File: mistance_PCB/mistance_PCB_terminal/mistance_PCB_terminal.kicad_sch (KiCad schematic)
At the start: 51 parts, among them J1 SMA-J-P-X-ST-TH1, Q1 Q_PMOS_DSG, U1 AMS1117-3.3, U2 STM32F103C8T6, U3 MCP73831-2-OT, U4 CP2104, U5 TPS61200DRC, U6 USBLC6-2P6, U7 SX1278, Y1 Crystal

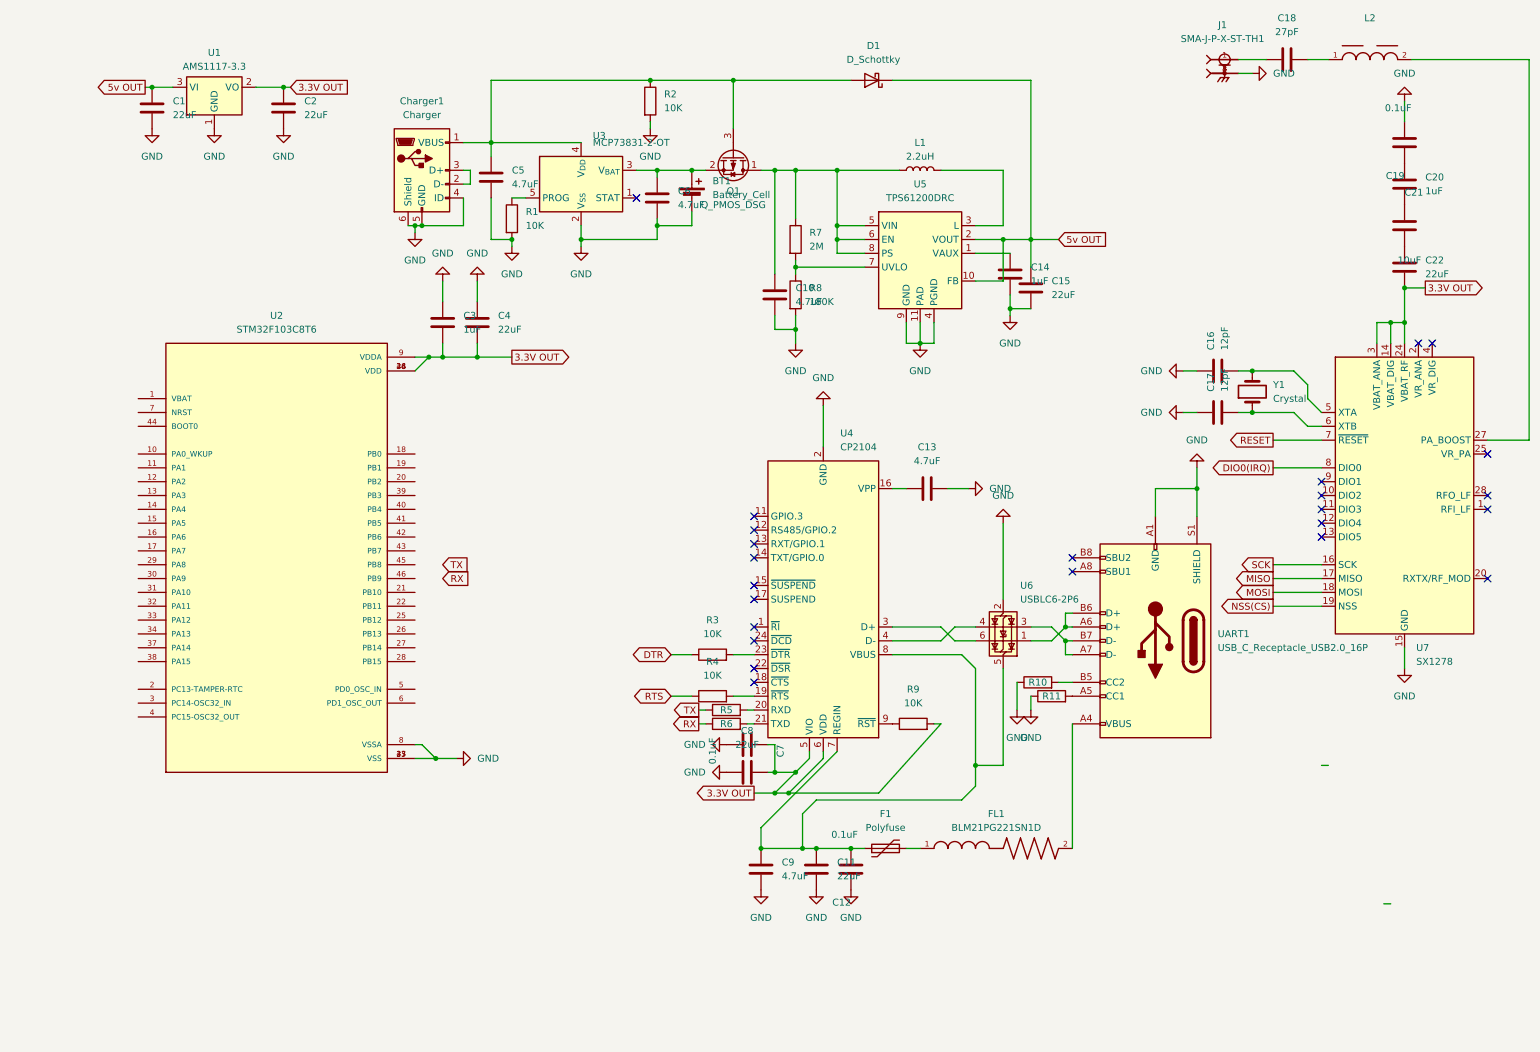
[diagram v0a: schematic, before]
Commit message: modify terminal SCH
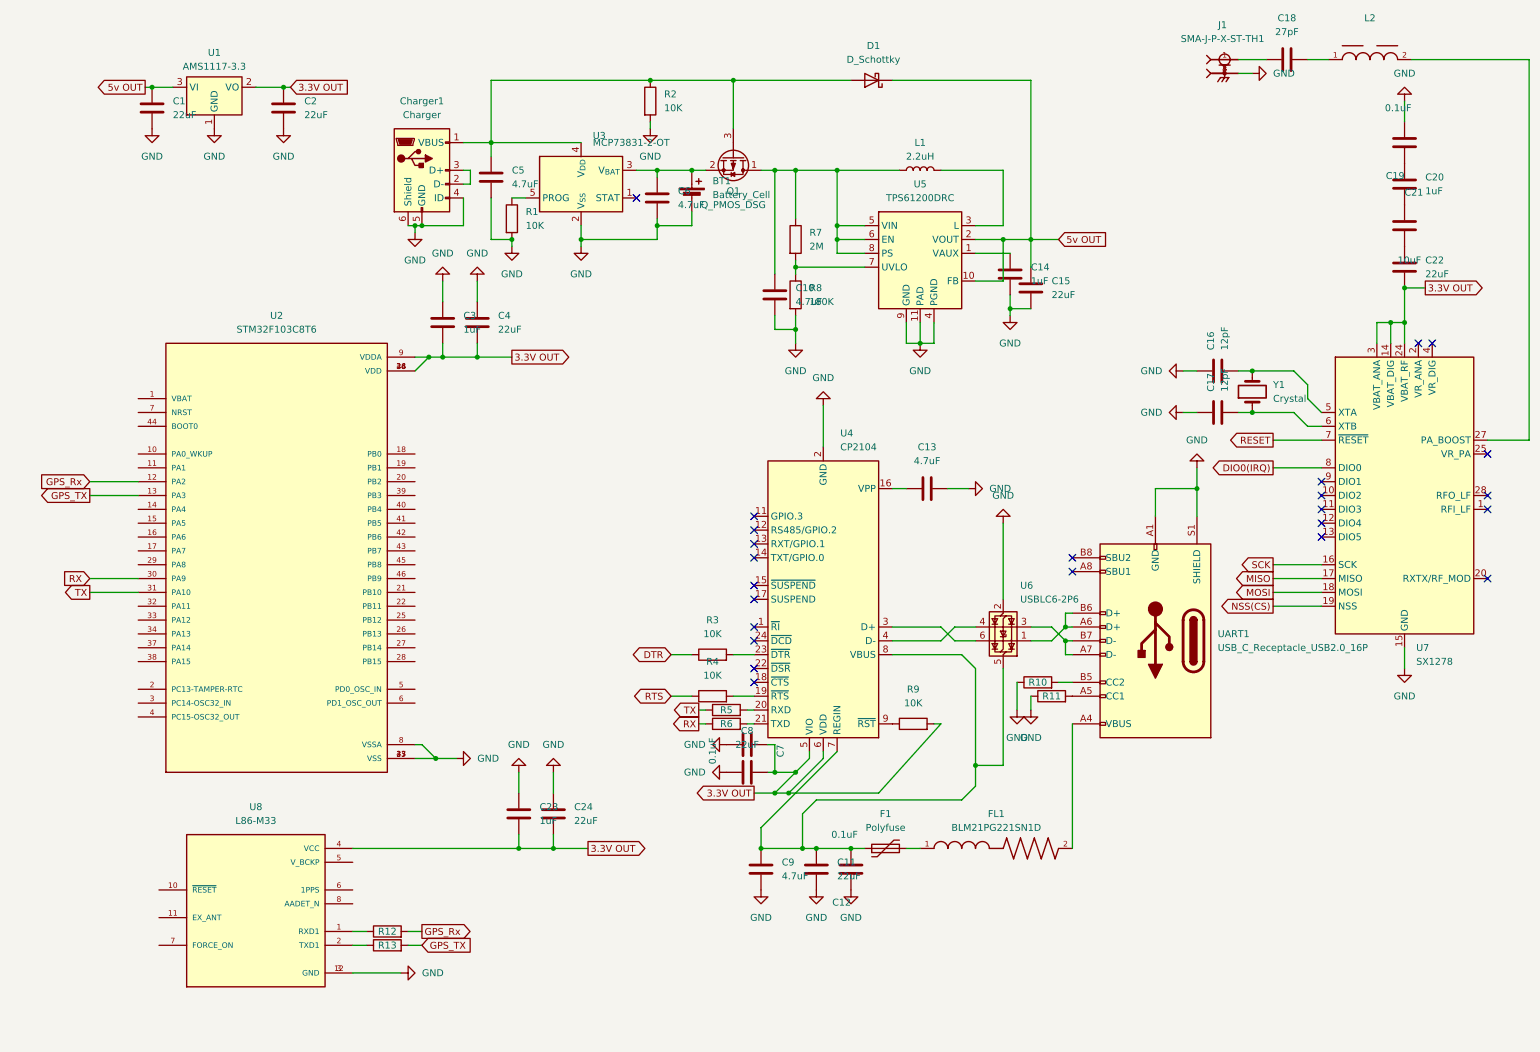
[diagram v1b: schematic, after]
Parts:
- added C23: 1uF, Capacitor_SMD:C_0603_1608Metric, symbol Device:C
- added C24: 22uF, Capacitor_SMD:C_0805_2012Metric, symbol Device:C
- added R12, R13: 22R, Resistor_SMD:R_0402_1005Metric, symbol Device:R
- added U8: L86-M33, L86-M33:XCVR_L86-M33, symbol L86-M33:L86-M33
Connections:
- net 3.3V OUT: now also C23.2, C24.2, U8.4 (VCC)
- net GND: now also C23.1, C24.1, U8.12 (GND), U8.3 (GND)
- net RX: now also U2.30 (PA9)
- net TX: now also U2.31 (PA10)
- net GPS_Rx: now reaches U2.12 (PA2)
- net GPS_Rx: now also R12.2
- net GPS_TX: now reaches U2.13 (PA3)
- net GPS_TX: now also R13.2
- new net: R12.1, U8.1 (RXD1)
- new net: R13.1, U8.2 (TXD1)

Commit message: modify terminal SCH
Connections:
- net 3.3V OUT: now also U8.5 (V_BCKP)
- net GPS_Reset: now reaches U2.11 (PA1)
- net GPS_Reset: now also U8.10 (~{RESET})
- no-connect marks 24 -> 28
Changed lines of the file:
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@@
+	)
+	(junction
+		(at 68.58 161.29)
+		(diameter 0)
+		(color 0 0 0 0)
 	)
 	(junction
@@
 	)
 	(no_connect
+		(at 66.04 168.91)
+	)
+	(no_connect
 		(at 274.32 111.76)
 	)
@@
 	)
 	(no_connect
+		(at 66.04 171.45)
+	)
+	(no_connect
 		(at 274.32 96.52)
 	)
@@
 	)
 	(no_connect
+		(at 30.48 173.99)
+	)
+	(no_connect
 		(at 139.7 123.19)
 	)
 	(no_connect
+		(at 30.48 179.07)
+	)
+	(no_connect
 		(at 243.84 93.98)
 	)
@@
 	(wire
 		(pts
-			(xy 66.04 161.29) (xy 96.52 161.29)
+			(xy 66.04 161.29) (xy 68.58 161.29)
 		)
 		(stroke
@@
 	(wire
 		(pts
+			(xy 68.58 161.29) (xy 96.52 161.29)
+		)
+		(stroke
+			(width 0)
+			(type default)
+		)
+	)
+	(wire
+		(pts
 			(xy 152.4 80.01) (xy 152.4 87.63)
 		)
@@
 	(wire
 		(pts
+			(xy 68.58 161.29) (xy 66.04 163.83)
+		)
+		(stroke
+			(width 0)
+			(type default)
+		)
+	)
+	(wire
+		(pts
 			(xy 95.25 41.91) (xy 97.79 41.91)
 		)
@@
 	(wire
 		(pts
+			(xy 25.4 168.91) (xy 30.48 168.91)
+		)
+		(stroke
+			(width 0)
+			(type default)
+		)
+	)
+	(wire
+		(pts
 			(xy 81.28 144.78) (xy 85.09 144.78)
 		)
@@
 		(pts
 			(xy 180.34 52.07) (xy 186.69 52.07)
+		)
+		(stroke
+			(width 0)
+			(type default)
+		)
+	)
+	(wire
+		(pts
+			(xy 17.78 91.44) (xy 26.67 91.44)
 		)
 		(stroke
@@
 	)
 	(global_label "TX"
-		(shape output)
+		(shape input)
 		(at 17.78 114.3 180)
 		(fields_autoplaced yes)
@@
 	)
 	(global_label "RX"
-		(shape input)
+		(shape output)
 		(at 17.78 111.76 180)
 		(fields_autoplaced yes)
@@
 		)
 	)
+	(global_label "GPS_Reset"
+		(shape input)
+		(at 17.78 91.44 180)
+		(fields_autoplaced yes)
+		(effects
+			(font
+				(size 1.27 1.27)
+			)
+			(justify right)
+		)
+		(property "Intersheetrefs" "${INTERSHEET_REFS}"
+			(at 4.8767 91.44 0)
+			(effects
+				(font
+					(size 1.27 1.27)
+				)
+				(justify right)
+				(hide yes)
+			)
+		)
+	)
 	(global_label "MISO"
 		(shape output)
@@
 		)
 	)
+	(global_label "GPS_Reset"
+		(shape output)
+		(at 25.4 168.91 180)
+		(fields_autoplaced yes)
+		(effects
+			(font
+				(size 1.27 1.27)
+			)
+			(justify right)
+		)
+		(property "Intersheetrefs" "${INTERSHEET_REFS}"
+			(at 12.4967 168.91 0)
+			(effects
+				(font
+					(size 1.27 1.27)
+				)
+				(justify right)
+				(hide yes)
+			)
+		)
+	)
 	(global_label "RTS"
 		(shape bidirectional)
@@
 	)
 	(global_label "RX"
-		(shape output)
+		(shape input)
 		(at 129.54 138.43 180)
 		(fields_autoplaced yes)

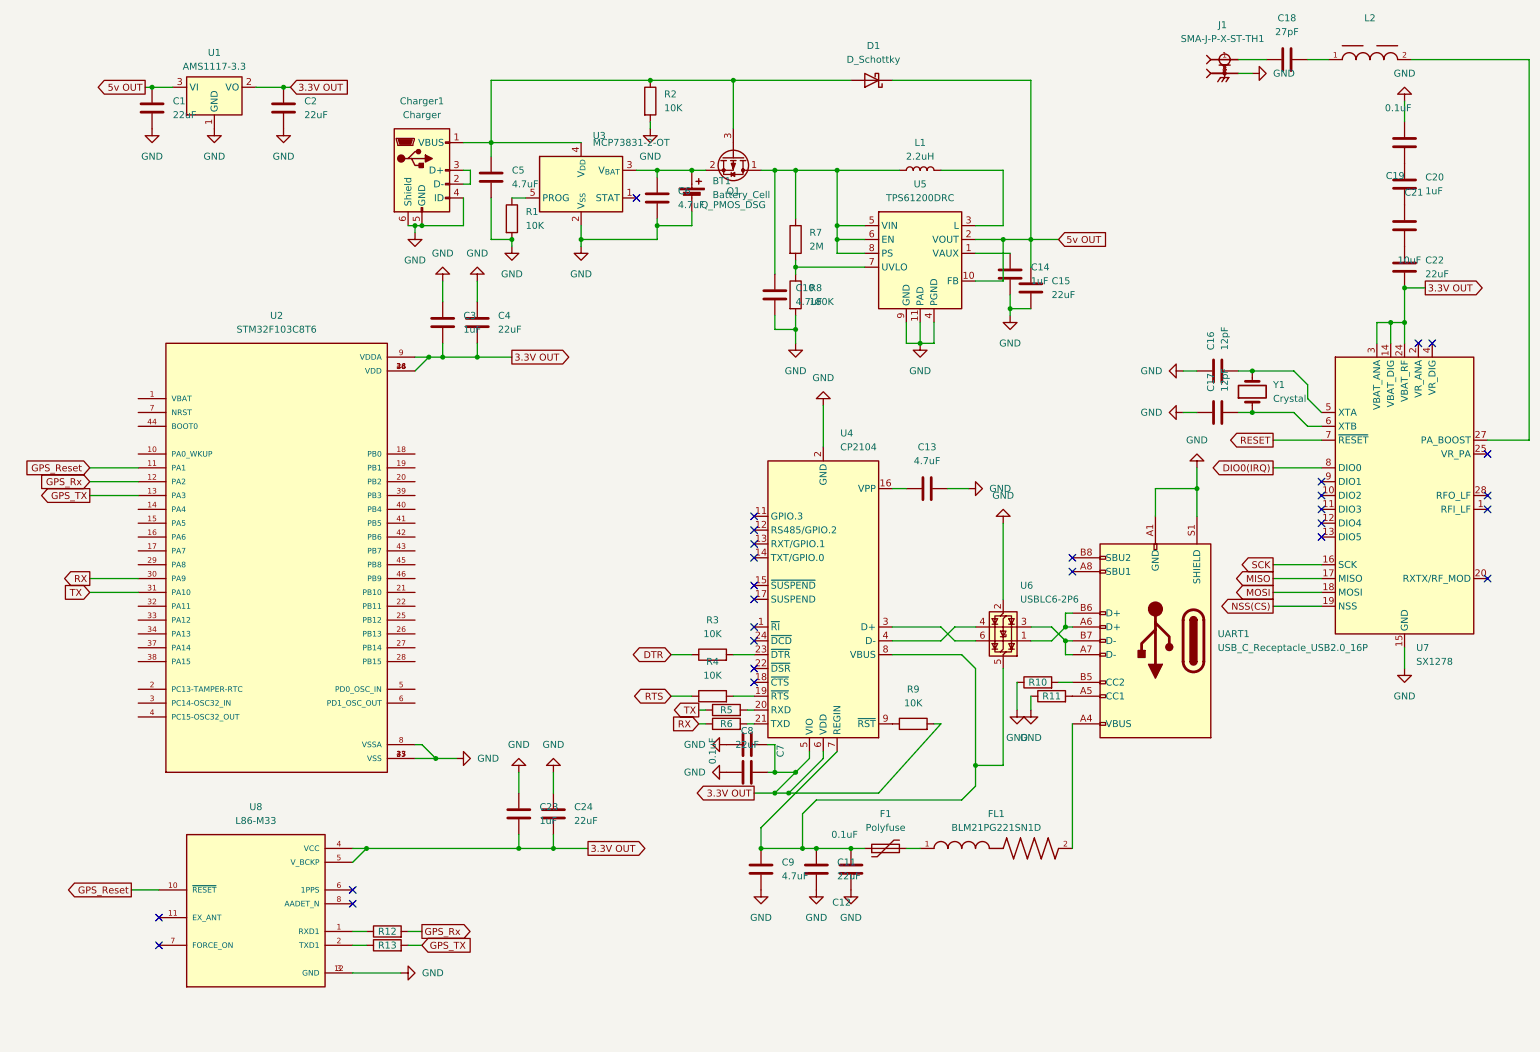
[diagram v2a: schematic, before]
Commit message: modify terminal SCH
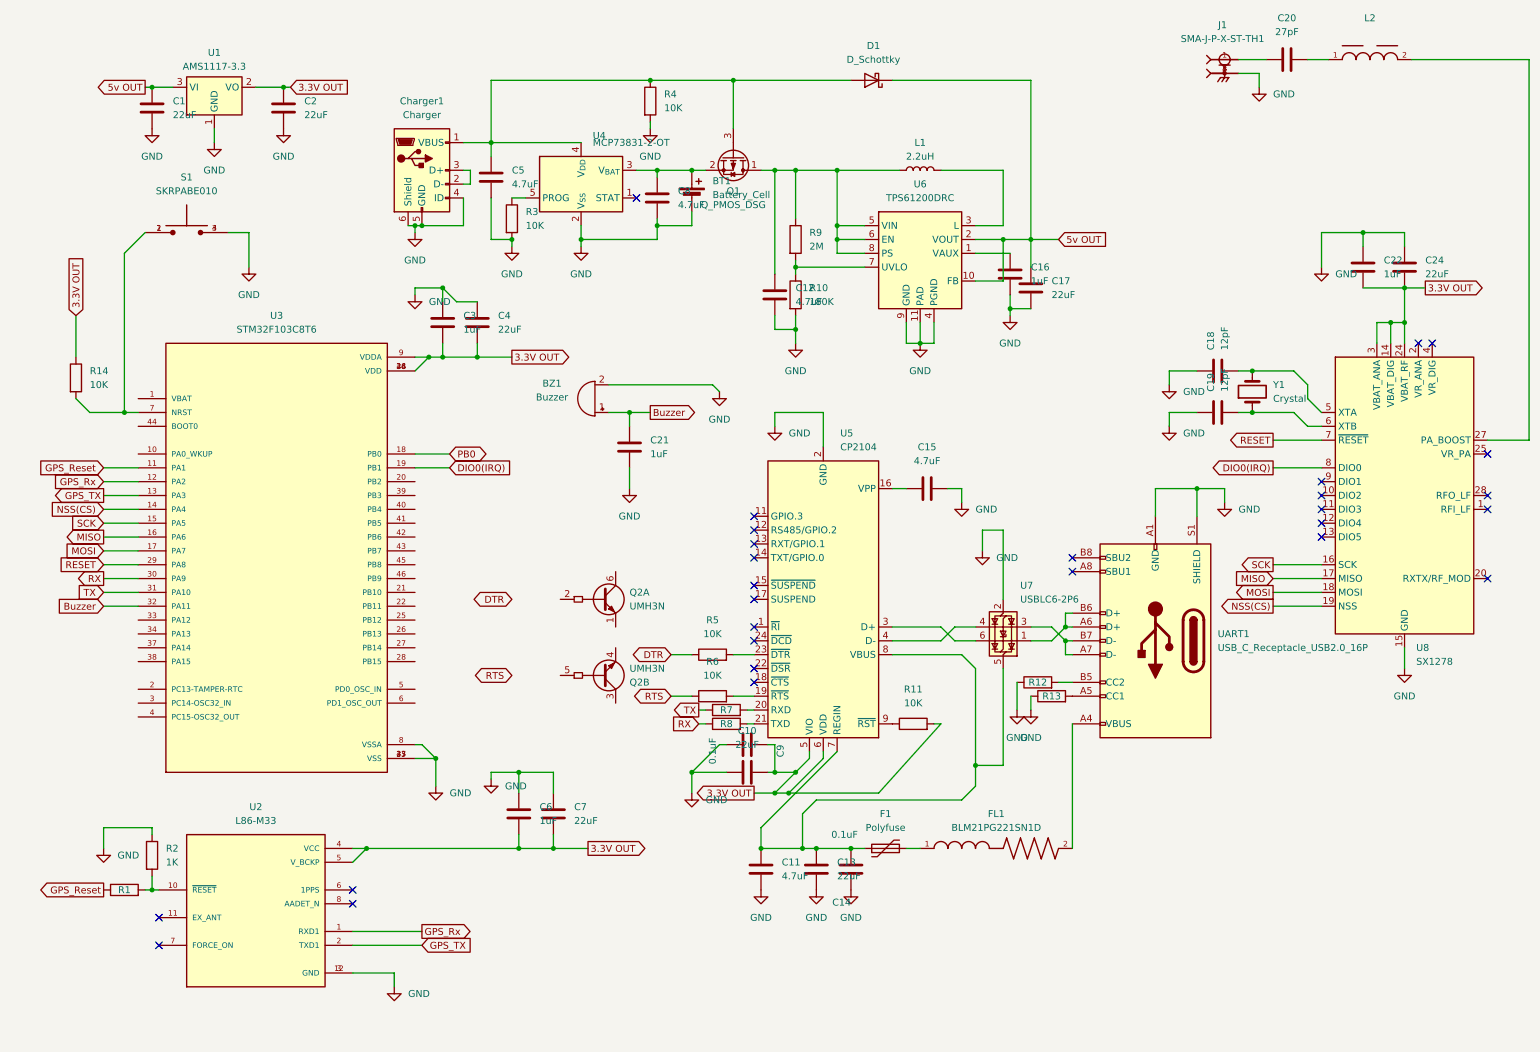
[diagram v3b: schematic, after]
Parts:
- removed C19: 0.1uF, Capacitor_SMD:C_0603_1608Metric, symbol Device:C
- removed R12, R13: 22R, Resistor_SMD:R_0402_1005Metric, symbol Device:R
- added BZ1: Buzzer, symbol Device:Buzzer
- added Q2: UMH3N, Package_TO_SOT_SMD:SOT-363_SC-70-6, symbol Transistor_BJT:UMH3N
- added R1: 100R, Resistor_SMD:R_0402_1005Metric, symbol Device:R
- added R14: 10K, Resistor_SMD:R_0603_1608Metric, symbol Device:R
- added R2: 1K, Resistor_SMD:R_0603_1608Metric, symbol Device:R
- added S1: SKRPABE010, Diode_SMD:SW_SKRPABE010, symbol SKRPABE010:SKRPABE010
- C21: value 10uF -> 1uF
- renumbered C8 to C10, C9 to C11, C10 to C12, C11 to C13, C12 to C14, C13 to C15, C14 to C16, C15 to C17, C16 to C18, C17 to C19, C18 to C20, C20 to C22, C22 to C24, C23 to C6, C24 to C7, C6 to C8, C7 to C9, R8 to R10, R9 to R11, R10 to R12, R11 to R13, R1 to R3, R2 to R4, R3 to R5, R4 to R6, R5 to R7, R6 to R8, R7 to R9, U8 to U2, U2 to U3, U3 to U4, U4 to U5, U5 to U6, U6 to U7, U7 to U8
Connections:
- net 3.3V OUT: now also C22.2, R14.1
- net DIO0(IRQ): now also U3.19 (PB1)
- net GND: now also C21.2, C22.1, C24.1, BZ1.2 (-), R2.1, S1.3, S1.4
- net GPS_Reset: now also R1.1; no longer U2.10 (~{RESET})
- net GPS_Rx: now also U2.1 (RXD1)
- net GPS_TX: now also U2.2 (TXD1)
- net MISO: now also U3.16 (PA6)
- net MOSI: now also U3.17 (PA7)
- net NSS(CS): now also U3.14 (PA4)
- net RESET: now also U3.29 (PA8)
- net SCK: now also U3.15 (PA5)
- net PB0: now reaches U3.18 (PB0)
- net Buzzer: now reaches U3.32 (PA11)
- net Buzzer: now also C21.1, BZ1.1 (+)
- net at U3.7 (NRST): now also R14.2, S1.1, S1.2
- new net: R1.2, R2.2, U2.10 (~{RESET})
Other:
- moved on the sheet: C22

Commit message: modify terminal SCH
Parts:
- added C23, C25: 20pF, Capacitor_SMD:C_0402_1005Metric, symbol Device:C
- added R15: 1M, Resistor_SMD:R_0603_1608Metric, symbol Device:R
- added Y2: ABM3B-8.000MHZ-B2-T, ABM3B-8.000MHZ-B2-T:XTAL_ABM3B-8.000MHZ-B2-T, symbol ABM3B-8.000MHZ-B2-T:ABM3B-8.000MHZ-B2-T
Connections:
- net GND: now also Y2.2 (GND), Y2.4 (GND)
- net OSC32_IN: now reaches U3.3 (PC14-OSC32_IN)
- net OSC32_OUT: now reaches U3.4 (PC15-OSC32_OUT)
- net OSC_IN: now reaches U3.5 (PD0_OSC_IN)
- net OSC_IN: now also C23.2, R15.1, Y2.3
- net OSC_OUT: now reaches U3.6 (PD1_OSC_OUT)
- net OSC_OUT: now also C25.2, R15.2, Y2.1
- new net: C23.1, C25.1

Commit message: PCB and code modify
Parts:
- added R16: 10K, Resistor_SMD:R_0603_1608Metric, symbol Device:R
- added S2: SKRPABE010, Diode_SMD:SW_SKRPABE010, symbol SKRPABE010:SKRPABE010
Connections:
- net 3.3V OUT: now also U3.1 (VBAT), S2.3, S2.4
- net DTR: now also Q2.2 (B1), Q2.4 (E2)
- net GND: now also R16.1, S2.1, S2.2
- net RTS: now also Q2.1 (E1), Q2.5 (B2)
- net NRST: now reaches R14.2, S1.1, S1.2, U3.7 (NRST)
- net NRST: now also Q2.3 (C2)
- net BOOT0: now reaches U3.44 (BOOT0)
- net BOOT0: now also Q2.6 (C1), R16.2
- net OSC32_IN: no longer names the net of U3.3 (PC14-OSC32_IN)
- net OSC32_OUT: no longer names the net of U3.4 (PC15-OSC32_OUT)
- no-connect marks 28 -> 50
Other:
- moved on the sheet: C3, C4, C6, C7, Q2A, R1, R14, R2, S1, U2, U3
